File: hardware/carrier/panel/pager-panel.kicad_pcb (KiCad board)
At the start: 2 copper layers, 32 x 20 mm, 26 parts, among them J1 GDEY029T94 FPC, J2 CARRIER, J3 FL-A FPC (FL03), J5 FRONTLIGHT, Q5 SI1308EDL

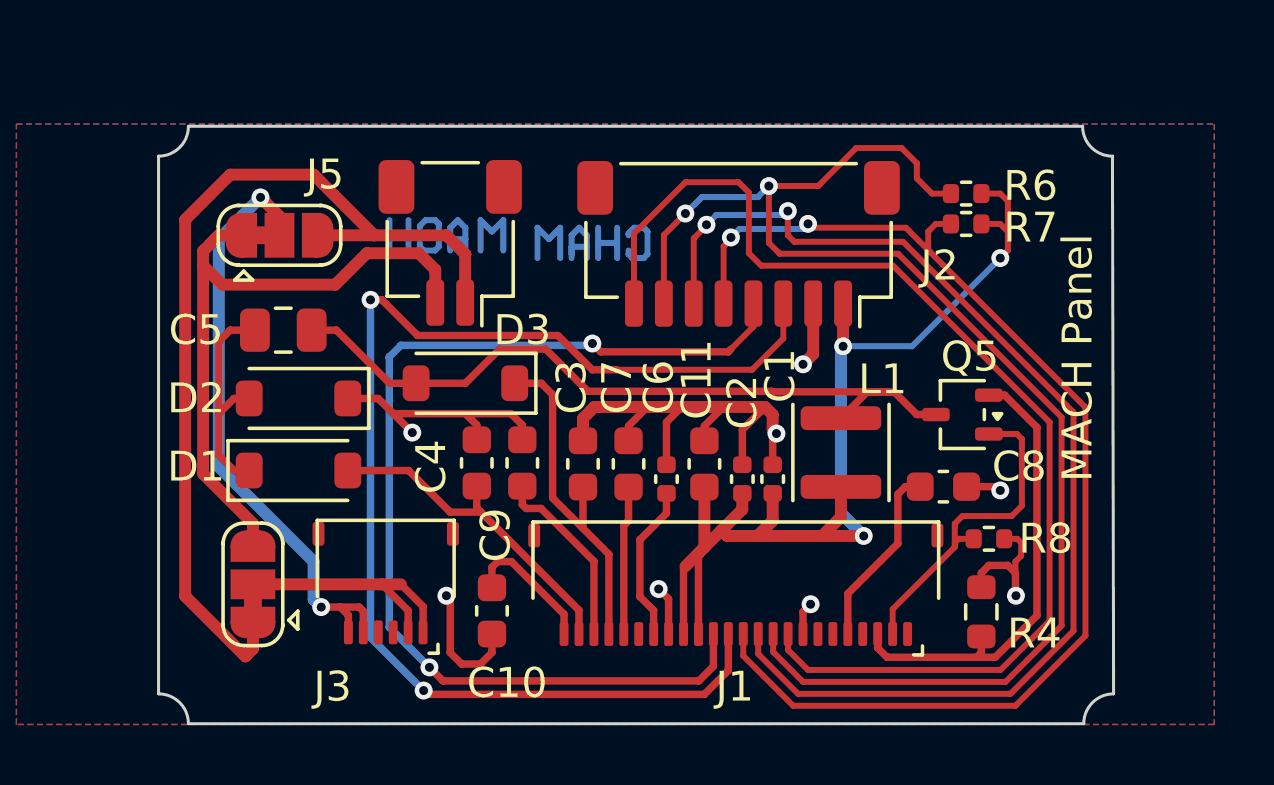
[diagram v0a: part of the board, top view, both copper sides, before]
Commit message: Panel: J1/J3 to SnapEDA FH34SRJ footprints (hold-downs at 2.5 mm, pin 1 per Hirose)
JLC flagged J1/J3: the custom footprints put the MP pads at y=3.3
(read the datasheet's 3.3 outer-edge span as centre-to-centre) and
had pin 1 mirrored.

Co-Authored-By: Claude Opus 5.5 <noreply@anthropic.com>
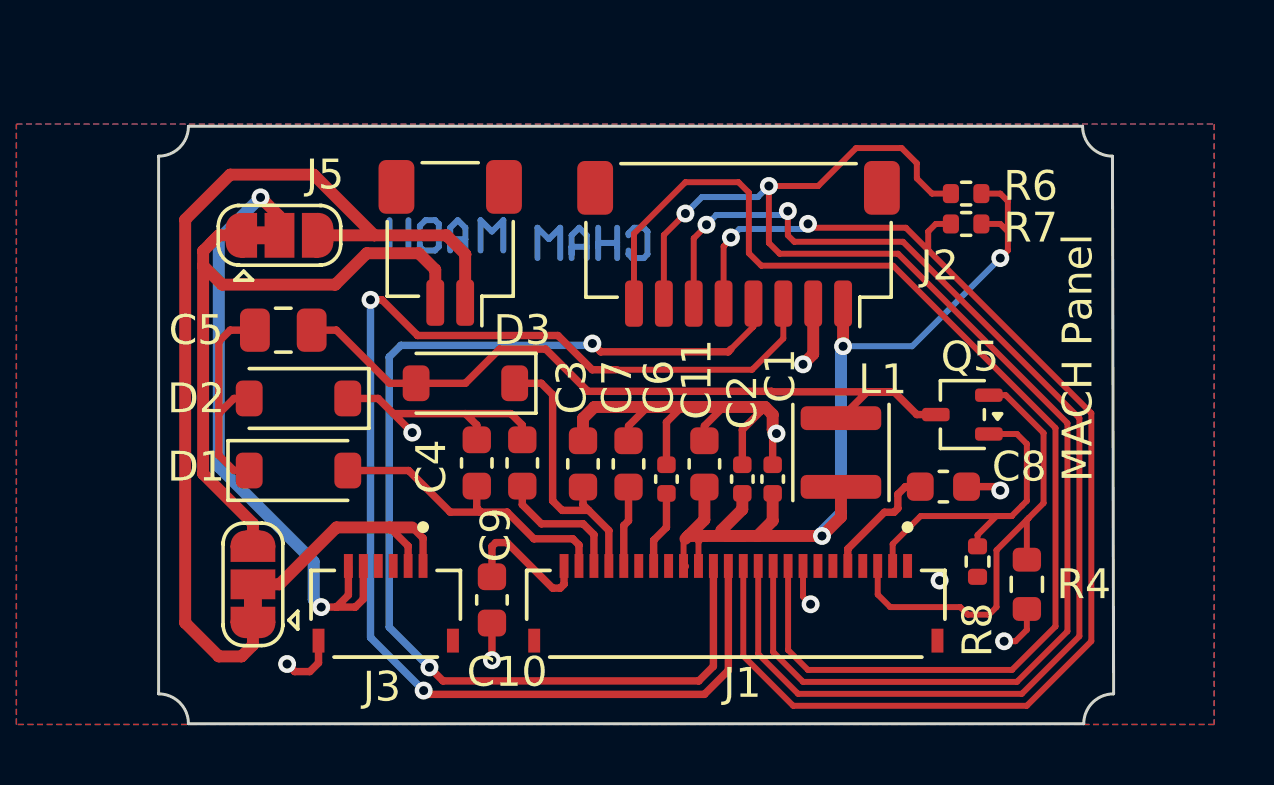
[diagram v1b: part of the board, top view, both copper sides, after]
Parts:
- J1: value GDEY029T94 FPC -> FH34SRJ-24S-0.5SH_50_; footprint pager-carrier:Hirose_FH34SRJ-24S-0.5SH_1x24-1MP_P0.50mm_Horizontal -> h24:HRS_FH34SRJ-24S-0.5SH_50_
- J3: value FL-A FPC (FL03) -> FH34SRJ-6S-0.5SH_50_; footprint pager-carrier:Hirose_FH34SRJ-6S-0.5SH_1x06-1MP_P0.50mm_Horizontal -> h6:HRS_FH34SRJ-6S-0.5SH_50_
- moved R4 1.78 mm to (112.1, 69.8), turned to -90 degrees
- moved J1 1.03 mm to (102.4, 70.5), turned to 0 degrees
- moved J3 0.97 mm to (90.7, 70.5), turned to 0 degrees
- moved R8 0.85 mm to (110.5, 69.1), turned to -90 degrees
- moved C10 0.37 mm to (94.2, 70.4)
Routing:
- net GND: track 39.6 -> 34.5 mm, vias 8 -> 9
- net 3V3_EPD: track 36.9 -> 32.9 mm
- net /panel/EINK_CS: track 39.9 -> 42.6 mm
- net /panel/EINK_RST: track 46.6 -> 49.3 mm
- net /panel/EINK_DC: track 38.5 -> 41.2 mm
- net /panel/EINK_BUSY: track 38.4 -> 41.1 mm
- net /panel/EPD_VDD: track 5.27 -> 2.61 mm
- net /panel/EPD_VGH: track 11.6 -> 9.32 mm
- net /panel/EPD_VSH1: track 4.99 -> 2.71 mm
- net /panel/EINK_SCK: track 42.0 -> 44.3 mm
- net /panel/EINK_MOSI: track 35.5 -> 37.8 mm
- net /panel/EPD_VSH2: track 6.23 -> 4.27 mm
- net /panel/EPD_VSL: track 6.24 -> 4.48 mm
- net FL_K: track 20.4 -> 21.4 mm
- net /panel/EPD_VGL: track 11.4 -> 10.4 mm

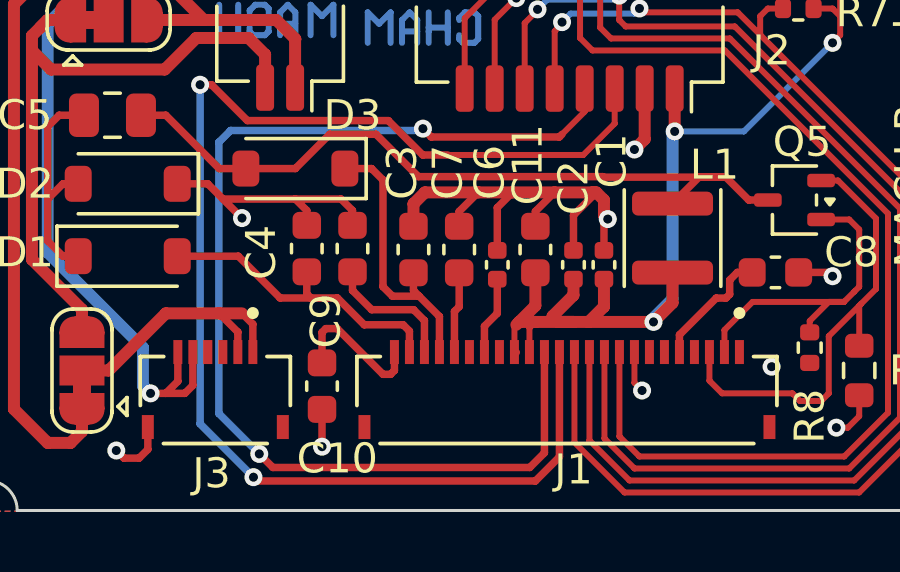
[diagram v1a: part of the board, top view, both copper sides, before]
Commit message: Panel: J1/J3 paste + mask fixes, bottom GND test pad, regenerated JLC files
SnapEDA FH34SRJ footprints had no F.Paste on the signal pads and a
0.102 mm per-pad mask margin that merged every opening at 0.5 mm
pitch (25 mask-bridge DRC errors). Signal pads now get paste
(-0.025 margin, 0.25 mm wide per Hirose stencil) and use the board's
0.05 mask margin.

TP1: 1 mm GND pad on B.Cu (board-only) so B_Mask.gbs is not empty;
JLC read the empty bottom mask as no solder mask.

Co-Authored-By: Claude Opus 5.5 <noreply@anthropic.com>
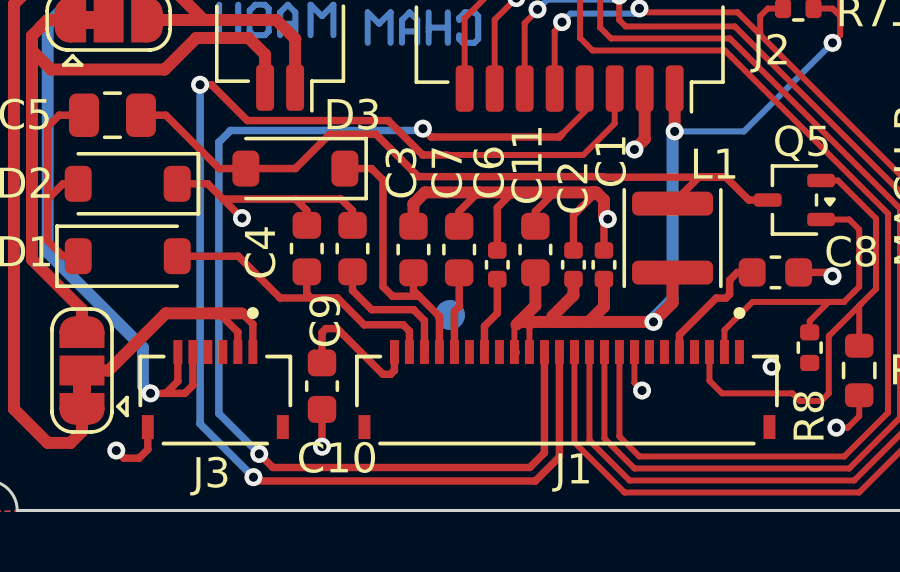
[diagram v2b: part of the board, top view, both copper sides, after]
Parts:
- added TP1: GND, TestPoint:TestPoint_Pad_D1.0mm, B.Cu at (98.5, 68.0)
